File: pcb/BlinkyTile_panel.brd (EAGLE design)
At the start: 220.1 x 170 mm, 216 parts

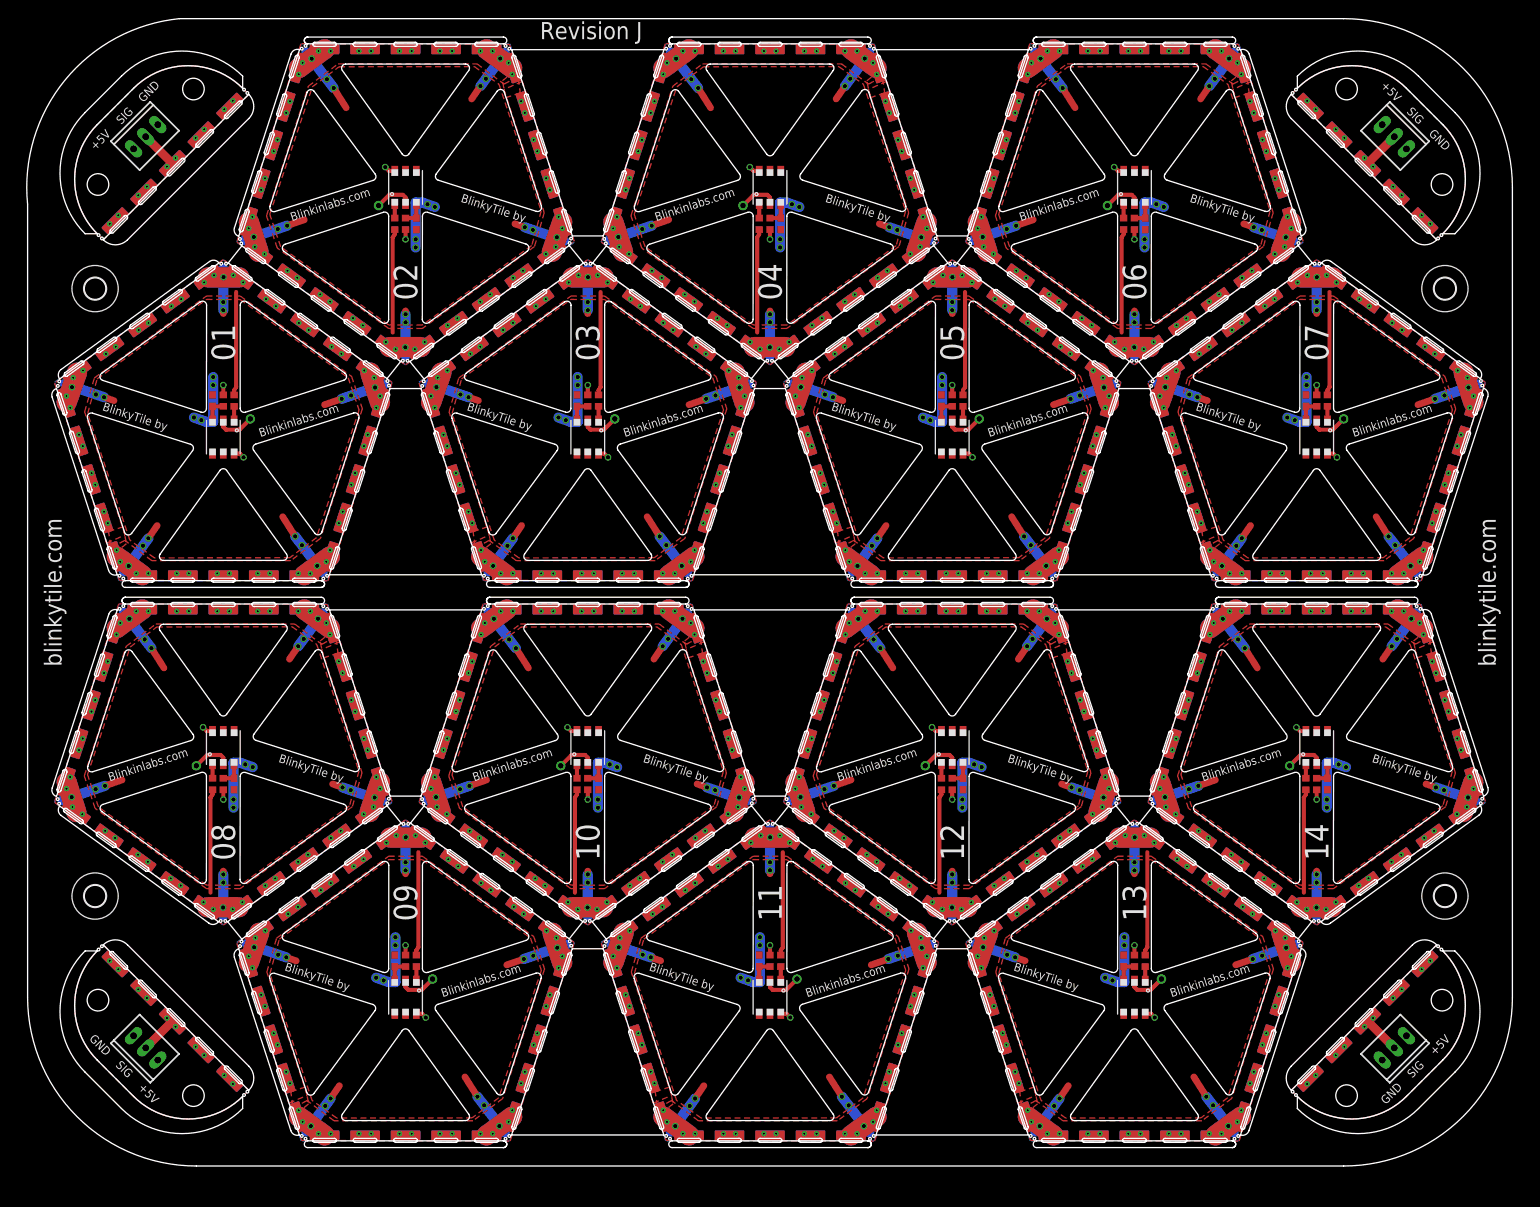
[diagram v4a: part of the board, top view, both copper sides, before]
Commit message: Updated controller and panel designs
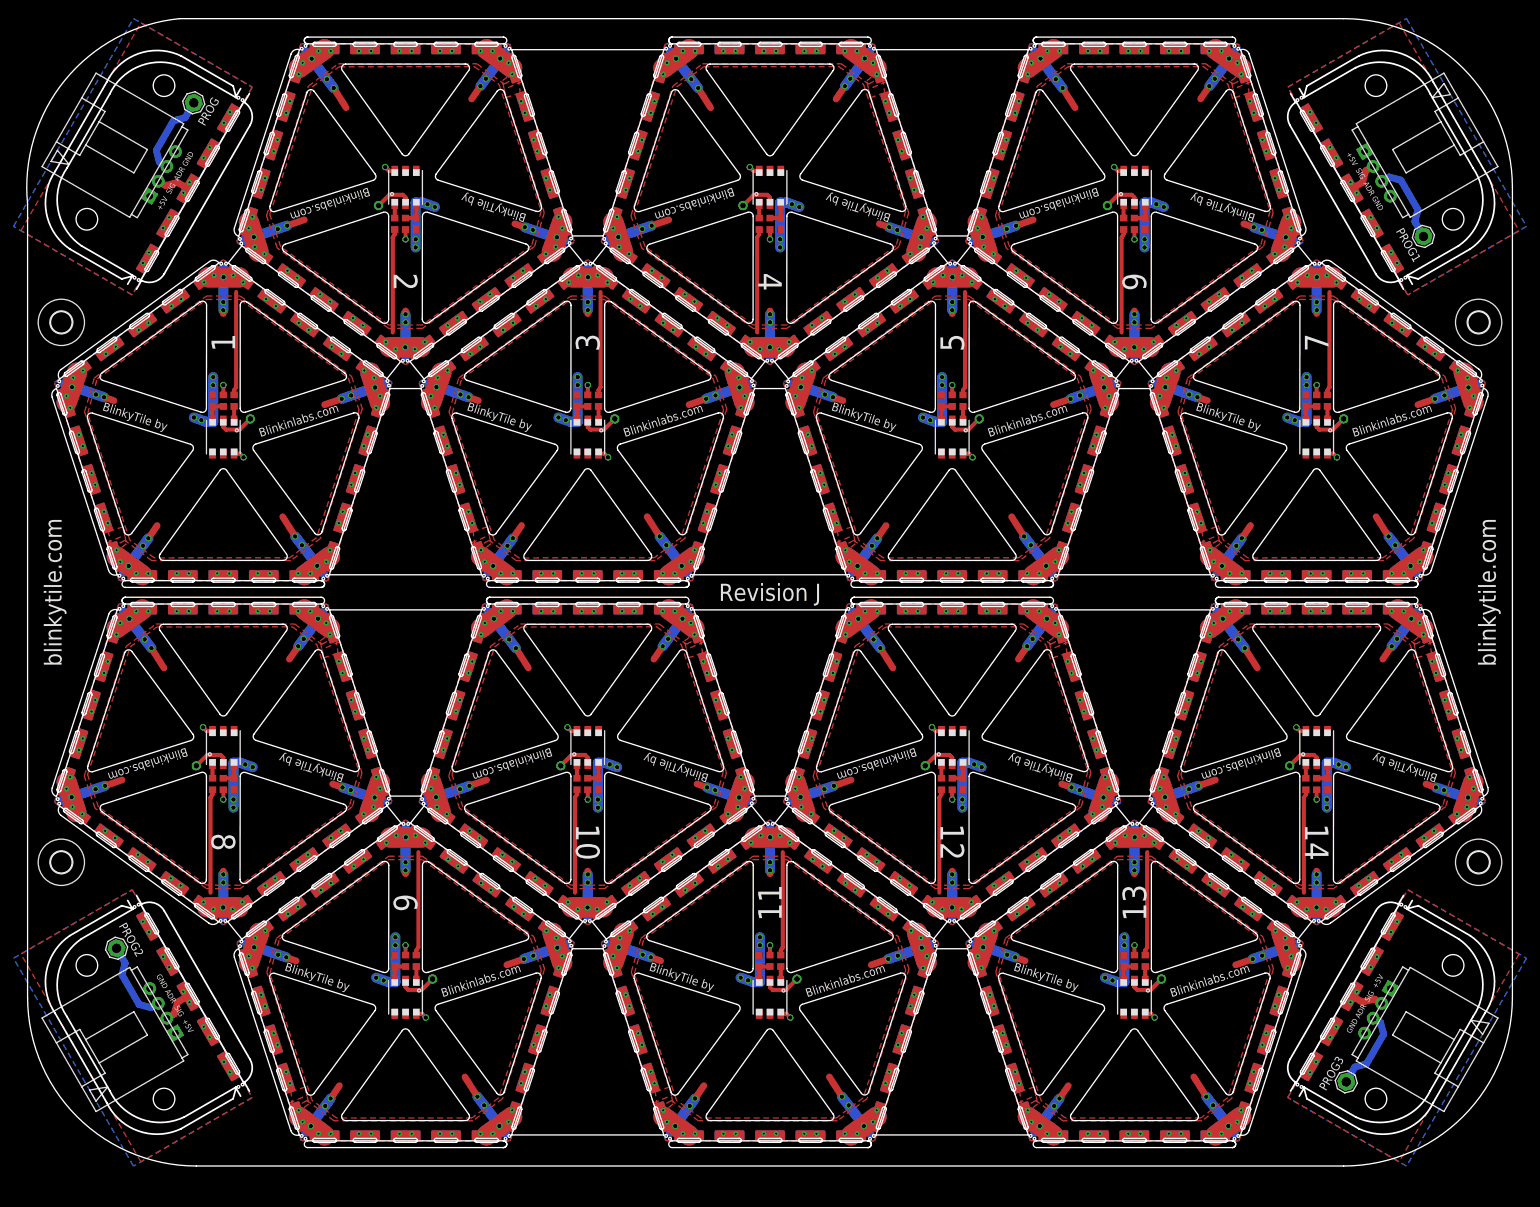
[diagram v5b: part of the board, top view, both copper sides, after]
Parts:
- removed E$83, E$84, E$86, E$87, E$89, E$90: (no value), dodocohedreled:MOUSE_BITE_1
- removed E$85, E$88: (no value), con-hdrs40:MTA-100-3V
- removed U$92, U$93, U$94, U$95: D_EDGEMOD, dodocohedreled:D_EDGE_SLOT_MOD
- added E$16, E$17, E$19, E$20, E$80, E$81: (no value), dodocohedreled:MOUSE_BITE
- added E$18, E$82: (no value), dodocohedreled:4-PIN_DUPONT
- added PROG, PROG1, PROG2, PROG3: (no value), solpad:SE14
- added U$19, U$20, U$21, U$91: D_EDGEMOD, dodocohedreled:D_EDGE_SLOT_MOD
- E$76, E$79: device con-hdrs40:MTA-100-3V -> dodocohedreled:4-PIN_DUPONT
- E$77, E$78: device dodocohedreled:MOUSE_BITE_1 -> dodocohedreled:MOUSE_BITE
- moved E$79 223.8 mm to (-90.0, -62.0), turned to 120 degrees
- moved E$76 182.6 mm to (90.0, 62.0), turned to 300 degrees
- moved E$77 127.4 mm to (-78.5, -73.0), turned to 210 degrees
- moved E$78 121.9 mm to (-93.8, -46.6), turned to 30 degrees
- moved E$91 7.07 mm to (-105.0, 40.0)
- moved E$92 7.07 mm to (-105.0, -40.0)
- moved E$93 7.07 mm to (105.0, -40.0)
- moved E$94 7.07 mm to (105.0, 40.0)
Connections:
- removed net S$13: E$88.2, U$95.P$3
- removed net S$14: E$88.3, U$95.P$1, U$95.P$5
- removed net S$15: E$88.1, U$95.P$7, U$95.P$9
- new net S$7: E$79.P$2, U$20.P$3
- new net S$8: E$79.P$3, PROG2.MP
- new net S$9: E$82.P$4, U$21.P$1, U$21.P$5
- new net VCC: E$18.P$1, U$91.P$7, U$91.P$9
- new net VCC1: E$76.P$1, U$19.P$7, U$19.P$9
- new net VCC2: E$79.P$1, U$20.P$7, U$20.P$9
- new net VCC3: E$82.P$1, U$21.P$7, U$21.P$9
- net S$1: now also E$18.P$2, U$91.P$3; no longer E$76.2, U$92.P$3
- net S$10: now also E$18.P$3, PROG.MP; no longer E$85.2, U$94.P$3
- net S$11: now also E$82.P$2, U$21.P$3; no longer E$85.3, U$94.P$1, U$94.P$5
- net S$12: now also E$82.P$3, PROG3.MP; no longer E$85.1, U$94.P$7, U$94.P$9
- net S$2: now also E$18.P$4, U$91.P$1, U$91.P$5; no longer E$76.3, U$92.P$1, U$92.P$5
- net S$3: now also E$76.P$4, U$19.P$1, U$19.P$5; no longer E$76.1, U$92.P$7, U$92.P$9
- net S$4: now also E$76.P$2, U$19.P$3; no longer E$79.2, U$93.P$3
- net S$5: now also E$76.P$3, PROG1.MP; no longer E$79.3, U$93.P$1, U$93.P$5
- net S$6: now also E$79.P$4, U$20.P$1, U$20.P$5; no longer E$79.1, U$93.P$7, U$93.P$9
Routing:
- net S$8: track 0.00 -> 12.5 mm
- net S$12: track 0.00 -> 12.5 mm
- net S$5: track 0.00 -> 12.5 mm
- net S$10: track 5.62 -> 12.5 mm
- net S$13: track 5.62 -> 0.00 mm
- net S$7: track 0.00 -> 4.88 mm
- net S$11: track 0.00 -> 4.88 mm
- net S$4: track 5.62 -> 4.88 mm
- net S$1: track 5.62 -> 4.88 mm
- added copper zone on layer 1, net S$3
- added copper zone on layer 1, net S$6
- added copper zone on layer 1, net S$9
- added copper zone on layer 16, net VCC
- added copper zone on layer 16, net VCC1
- added copper zone on layer 16, net VCC2
- added copper zone on layer 16, net VCC3
- removed copper zone on layer 1, net S$11
- removed copper zone on layer 16, net S$12
- removed copper zone on layer 1, net S$14
- removed copper zone on layer 16, net S$15
- removed copper zone on layer 16, net S$3
- removed copper zone on layer 1, net S$5
- removed copper zone on layer 16, net S$6
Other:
- outline, holes or cut-outs redrawn
- board text added: "1"
- board text added: "2"
- board text added: "3"
- board text added: "4"
- board text added: "5"
- board text added: "6"
- board text added: "7"
- board text added: "8"
- board text added: "9"
- board text added: "ADR"
- board text removed: "01"
- board text removed: "02"
- board text removed: "03"
- board text removed: "04"
- board text removed: "05"
- board text removed: "06"
- board text removed: "07"
- board text removed: "08"
- board text removed: "09"
